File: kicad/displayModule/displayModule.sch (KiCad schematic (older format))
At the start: 13 parts, among them J1 Connector, Q1 2N7000, Q2 2N7000, Q3 2N7000, Q4 2N7000, Q5 2N7000, Q6 2N7000, U1 ATtiny85-20PU, U2 74HC595, U3 74HC595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

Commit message: Begin work on display module printed pcb order
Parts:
- J1: footprint (none) -> Connector_PinHeader_2.54mm:PinHeader_1x04_P2.54mm_Vertical
- Q1, Q2, Q3, Q4, Q5, Q6: footprint Package_TO_SOT_THT:TO-92_Inline -> Package_TO_SOT_THT:TO-92_Inline_Wide
- R1: footprint (none) -> Resistor_THT:R_Axial_DIN0207_L6.3mm_D2.5mm_P7.62mm_Horizontal
- U2, U3: footprint (none) -> Package_DIP:DIP-16_W7.62mm
- U4, U5: footprint Display_7Segment:DE170-XX-XX -> displayModule:HDSP-433G
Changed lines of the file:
@@
 F 0 "U4" H 6780 2846 50  0000 L CNN
 F 1 "HDSP-433G" H 6780 2755 50  0000 L CNN
-F 2 "Display_7Segment:DE170-XX-XX" H 6400 1950 50  0001 C CNN
+F 2 "displayModule:HDSP-433G" H 6400 1950 50  0001 C CNN
 F 3 "" H 6200 2700 50  0001 C CNN
 	1    6400 2500
@@
 F 0 "U5" H 6780 4596 50  0000 L CNN
 F 1 "HDSP-433G" H 6780 4505 50  0000 L CNN
-F 2 "Display_7Segment:DE170-XX-XX" H 6400 3700 50  0001 C CNN
+F 2 "displayModule:HDSP-433G" H 6400 3700 50  0001 C CNN
 F 3 "" H 6200 4450 50  0001 C CNN
 	1    6400 4250
@@
 F 0 "U2" H 4250 2731 50  0000 C CNN
 F 1 "74HC595" H 4250 2640 50  0000 C CNN
-F 2 "" H 4250 1950 50  0001 C CNN
+F 2 "Package_DIP:DIP-16_W7.62mm" H 4250 1950 50  0001 C CNN
 F 3 "http://www.ti.com/lit/ds/symlink/sn74hc595.pdf" H 4250 1950 50  0001 C CNN
 	1    4250 1950
@@
 F 0 "U3" H 4300 4431 50  0000 C CNN
 F 1 "74HC595" H 4300 4340 50  0000 C CNN
-F 2 "" H 4300 3650 50  0001 C CNN
+F 2 "Package_DIP:DIP-16_W7.62mm" H 4300 3650 50  0001 C CNN
 F 3 "http://www.ti.com/lit/ds/symlink/sn74hc595.pdf" H 4300 3650 50  0001 C CNN
 	1    4300 3650
@@
 F 0 "J1" V 2112 744 50  0000 L CNN
 F 1 "Connector" V 2203 744 50  0000 L CNN
-F 2 "" H 2050 600 50  0001 C CNN
+F 2 "Connector_PinHeader_2.54mm:PinHeader_1x04_P2.54mm_Vertical" H 2050 600 50  0001 C CNN
 F 3 "~" H 2050 600 50  0001 C CNN
 	1    2050 600
@@
 $EndComp
 $Comp
-L power:GND #PWR?
+L power:GND #PWR04
 U 1 1 60F952A6
 P 2400 950
-F 0 "#PWR?" H 2400 700 50  0001 C CNN
+F 0 "#PWR04" H 2400 700 50  0001 C CNN
 F 1 "GND" H 2405 777 50  0000 C CNN
 F 2 "" H 2400 950 50  0001 C CNN
@@
 	2400 800  2400 950
 $Comp
-L power:+5V #PWR?
+L power:+5V #PWR03
 U 1 1 60F95DD0
 P 2150 950
-F 0 "#PWR?" H 2150 800 50  0001 C CNN
+F 0 "#PWR03" H 2150 800 50  0001 C CNN
 F 1 "+5V" H 2165 1123 50  0000 C CNN
 F 2 "" H 2150 950 50  0001 C CNN
@@
 	2950 1350 2950 2050
 $Comp
-L power:+5V #PWR?
+L power:+5V #PWR01
 U 1 1 60F9C62F
 P 2100 1550
-F 0 "#PWR?" H 2100 1400 50  0001 C CNN
+F 0 "#PWR01" H 2100 1400 50  0001 C CNN
 F 1 "+5V" V 2115 1678 50  0000 L CNN
 F 2 "" H 2100 1550 50  0001 C CNN
@@
 $EndComp
 $Comp
-L power:GND #PWR?
+L power:GND #PWR02
 U 1 1 60F9CC9A
 P 2100 2750
-F 0 "#PWR?" H 2100 2500 50  0001 C CNN
+F 0 "#PWR02" H 2100 2500 50  0001 C CNN
 F 1 "GND" V 2105 2622 50  0000 R CNN
 F 2 "" H 2100 2750 50  0001 C CNN
@@
 $EndComp
 $Comp
-L power:+5V #PWR?
+L power:+5V #PWR07
 U 1 1 60F9DD19
 P 4250 1350
-F 0 "#PWR?" H 4250 1200 50  0001 C CNN
+F 0 "#PWR07" H 4250 1200 50  0001 C CNN
 F 1 "+5V" V 4265 1478 50  0000 L CNN
 F 2 "" H 4250 1350 50  0001 C CNN
@@
 $EndComp
 $Comp
-L power:GND #PWR?
+L power:GND #PWR08
 U 1 1 60F9E92C
 P 4250 2650
-F 0 "#PWR?" H 4250 2400 50  0001 C CNN
+F 0 "#PWR08" H 4250 2400 50  0001 C CNN
 F 1 "GND" V 4255 2522 50  0000 R CNN
 F 2 "" H 4250 2650 50  0001 C CNN
@@
 $EndComp
 $Comp
-L power:+5V #PWR?
+L power:+5V #PWR09
 U 1 1 60F9F4CF
 P 4300 3050
-F 0 "#PWR?" H 4300 2900 50  0001 C CNN
+F 0 "#PWR09" H 4300 2900 50  0001 C CNN
 F 1 "+5V" V 4315 3178 50  0000 L CNN
 F 2 "" H 4300 3050 50  0001 C CNN
@@
 $EndComp
 $Comp
-L power:GND #PWR?
+L power:GND #PWR010
 U 1 1 60F9FF54
 P 4300 4350
-F 0 "#PWR?" H 4300 4100 50  0001 C CNN
+F 0 "#PWR010" H 4300 4100 50  0001 C CNN
 F 1 "GND" V 4305 4222 50  0000 R CNN
 F 2 "" H 4300 4350 50  0001 C CNN
@@
 	3550 1550 3850 1550
 $Comp
-L power:+5V #PWR?
+L power:+5V #PWR05
 U 1 1 60FB5E11
 P 3850 1850
-F 0 "#PWR?" H 3850 1700 50  0001 C CNN
+F 0 "#PWR05" H 3850 1700 50  0001 C CNN
 F 1 "+5V" V 3865 1978 50  0000 L CNN
 F 2 "" H 3850 1850 50  0001 C CNN
@@
 $EndComp
 $Comp
-L power:+5V #PWR?
+L power:+5V #PWR06
 U 1 1 60FB6557
 P 3900 3550
-F 0 "#PWR?" H 3900 3400 50  0001 C CNN
+F 0 "#PWR06" H 3900 3400 50  0001 C CNN
 F 1 "+5V" V 3915 3678 50  0000 L CNN
 F 2 "" H 3900 3550 50  0001 C CNN
@@
 	3750 3250 3900 3250
 $Comp
-L power:GND #PWR?
+L power:GND #PWR011
 U 1 1 60FCD7E2
 P 8550 2700
-F 0 "#PWR?" H 8550 2450 50  0001 C CNN
+F 0 "#PWR011" H 8550 2450 50  0001 C CNN
 F 1 "GND" V 8555 2572 50  0000 R CNN
 F 2 "" H 8550 2700 50  0001 C CNN
@@
 F 0 "Q1" V 8242 1500 50  0000 C CNN
 F 1 "2N7000" V 8151 1500 50  0000 C CNN
-F 2 "Package_TO_SOT_THT:TO-92_Inline" H 8100 1425 50  0001 L CIN
+F 2 "Package_TO_SOT_THT:TO-92_Inline_Wide" H 8100 1425 50  0001 L CIN
 F 3 "https://www.onsemi.com/pub/Collateral/NDS7002A-D.PDF" H 7900 1500 50  0001 L CNN
 	1    7900 1500
@@
 F 0 "Q2" V 8242 2150 50  0000 C CNN
 F 1 "2N7000" V 8151 2150 50  0000 C CNN
-F 2 "Package_TO_SOT_THT:TO-92_Inline" H 8100 2075 50  0001 L CIN
+F 2 "Package_TO_SOT_THT:TO-92_Inline_Wide" H 8100 2075 50  0001 L CIN
 F 3 "https://www.onsemi.com/pub/Collateral/NDS7002A-D.PDF" H 7900 2150 50  0001 L CNN
 	1    7900 2150
@@
 F 0 "Q3" V 8242 2800 50  0000 C CNN
 F 1 "2N7000" V 8151 2800 50  0000 C CNN
-F 2 "Package_TO_SOT_THT:TO-92_Inline" H 8100 2725 50  0001 L CIN
+F 2 "Package_TO_SOT_THT:TO-92_Inline_Wide" H 8100 2725 50  0001 L CIN
 F 3 "https://www.onsemi.com/pub/Collateral/NDS7002A-D.PDF" H 7900 2800 50  0001 L CNN
 	1    7900 2800
@@
 F 0 "Q4" V 8242 3450 50  0000 C CNN
 F 1 "2N7000" V 8151 3450 50  0000 C CNN
-F 2 "Package_TO_SOT_THT:TO-92_Inline" H 8100 3375 50  0001 L CIN
+F 2 "Package_TO_SOT_THT:TO-92_Inline_Wide" H 8100 3375 50  0001 L CIN
 F 3 "https://www.onsemi.com/pub/Collateral/NDS7002A-D.PDF" H 7900 3450 50  0001 L CNN
 	1    7900 3450
@@
 F 0 "Q5" V 8242 4100 50  0000 C CNN
 F 1 "2N7000" V 8151 4100 50  0000 C CNN
-F 2 "Package_TO_SOT_THT:TO-92_Inline" H 8100 4025 50  0001 L CIN
+F 2 "Package_TO_SOT_THT:TO-92_Inline_Wide" H 8100 4025 50  0001 L CIN
 F 3 "https://www.onsemi.com/pub/Collateral/NDS7002A-D.PDF" H 7900 4100 50  0001 L CNN
 	1    7900 4100
@@
 F 0 "Q6" V 8242 4750 50  0000 C CNN
 F 1 "2N7000" V 8151 4750 50  0000 C CNN
-F 2 "Package_TO_SOT_THT:TO-92_Inline" H 8100 4675 50  0001 L CIN
+F 2 "Package_TO_SOT_THT:TO-92_Inline_Wide" H 8100 4675 50  0001 L CIN
 F 3 "https://www.onsemi.com/pub/Collateral/NDS7002A-D.PDF" H 7900 4750 50  0001 L CNN
 	1    7900 4750
@@
 F 0 "R1" H 8470 2746 50  0000 L CNN
 F 1 "220" H 8470 2655 50  0000 L CNN
-F 2 "" V 8330 2700 50  0001 C CNN
+F 2 "Resistor_THT:R_Axial_DIN0207_L6.3mm_D2.5mm_P7.62mm_Horizontal" V 8330 2700 50  0001 C CNN
 F 3 "~" H 8400 2700 50  0001 C CNN
 	1    8400 2700

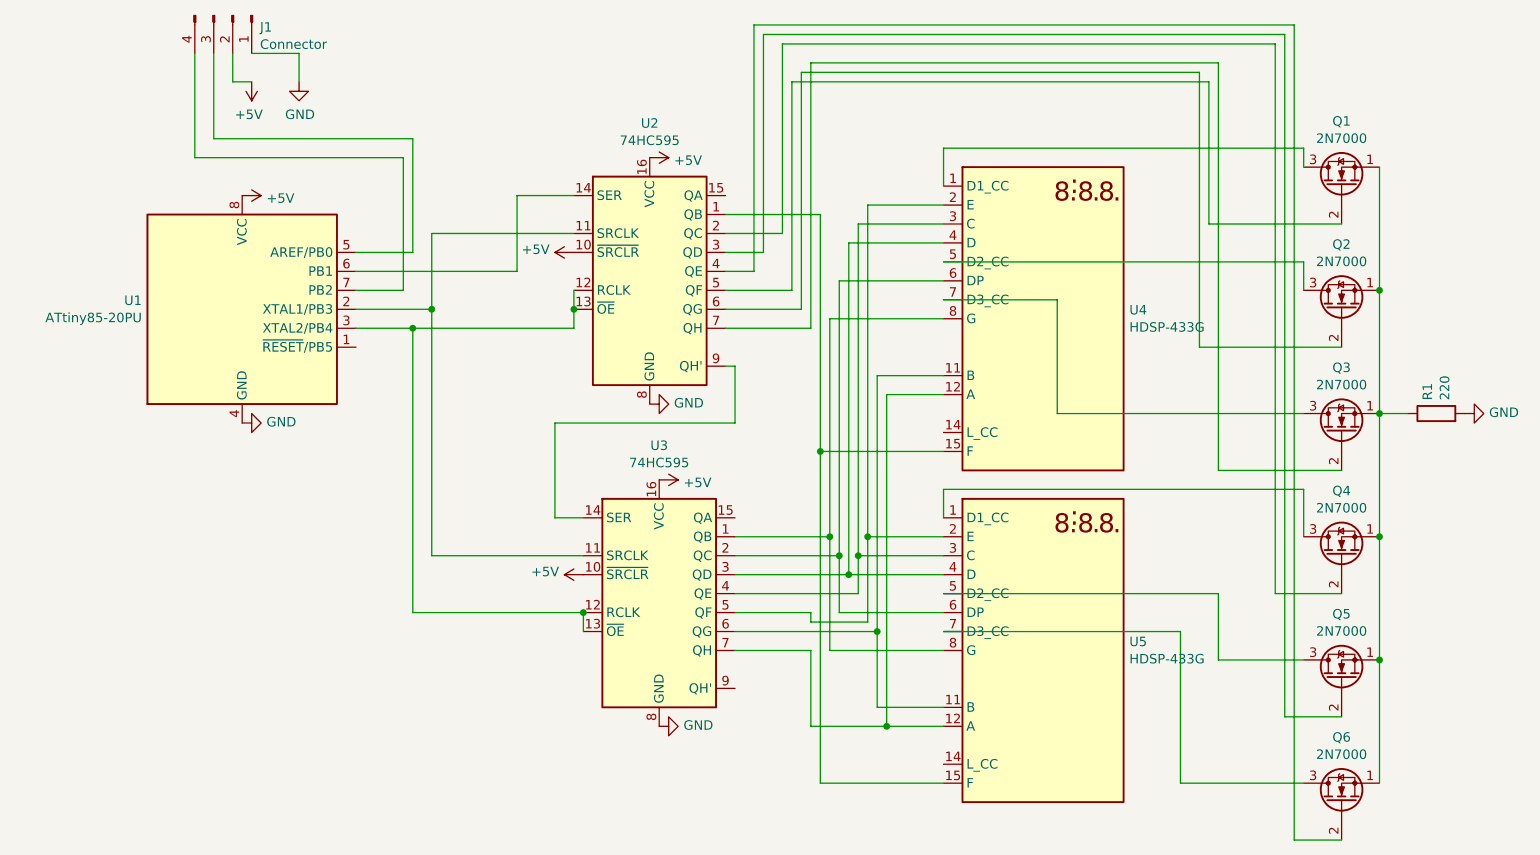
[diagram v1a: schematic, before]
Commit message: Only activate squelch after AM transmission is picked up
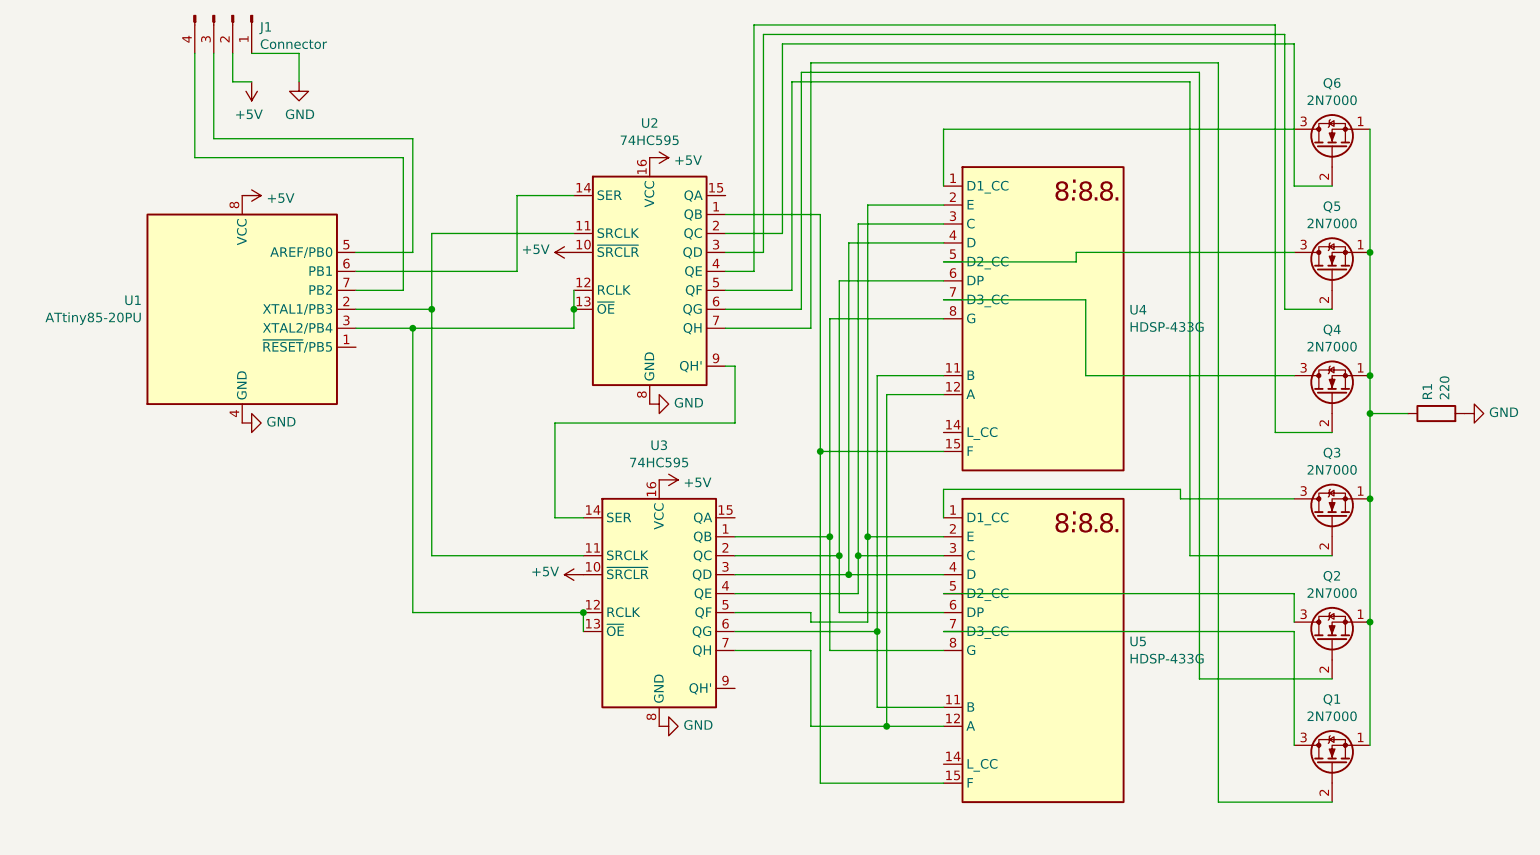
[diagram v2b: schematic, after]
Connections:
- net at U4.1 (D1_CC): now also Q6.3 (D); no longer Q1.3 (D)
- net at U4.5 (D2_CC): now also Q5.3 (D); no longer Q2.3 (D)
- net at U4.7 (D3_CC): now also Q4.3 (D); no longer Q3.3 (D)
- net at U5.1 (D1_CC): now also Q3.3 (D); no longer Q4.3 (D)
- net at U5.5 (D2_CC): now also Q2.3 (D); no longer Q5.3 (D)
- net at U5.7 (D3_CC): now also Q1.3 (D); no longer Q6.3 (D)
- net at U2.2 (QC): now also Q6.2 (G); no longer Q4.2 (G)
- net at U2.4 (QE): now also Q4.2 (G); no longer Q6.2 (G)
- net at U2.5 (QF): now also Q3.2 (G); no longer Q1.2 (G)
- net at U2.7 (QH): now also Q1.2 (G); no longer Q3.2 (G)
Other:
- moved on the sheet: Q1, Q2, Q3, Q4, Q5, Q6
